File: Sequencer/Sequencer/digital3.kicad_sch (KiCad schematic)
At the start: 3 parts, among them U6 40106, U7 CD4094, U8 TL072

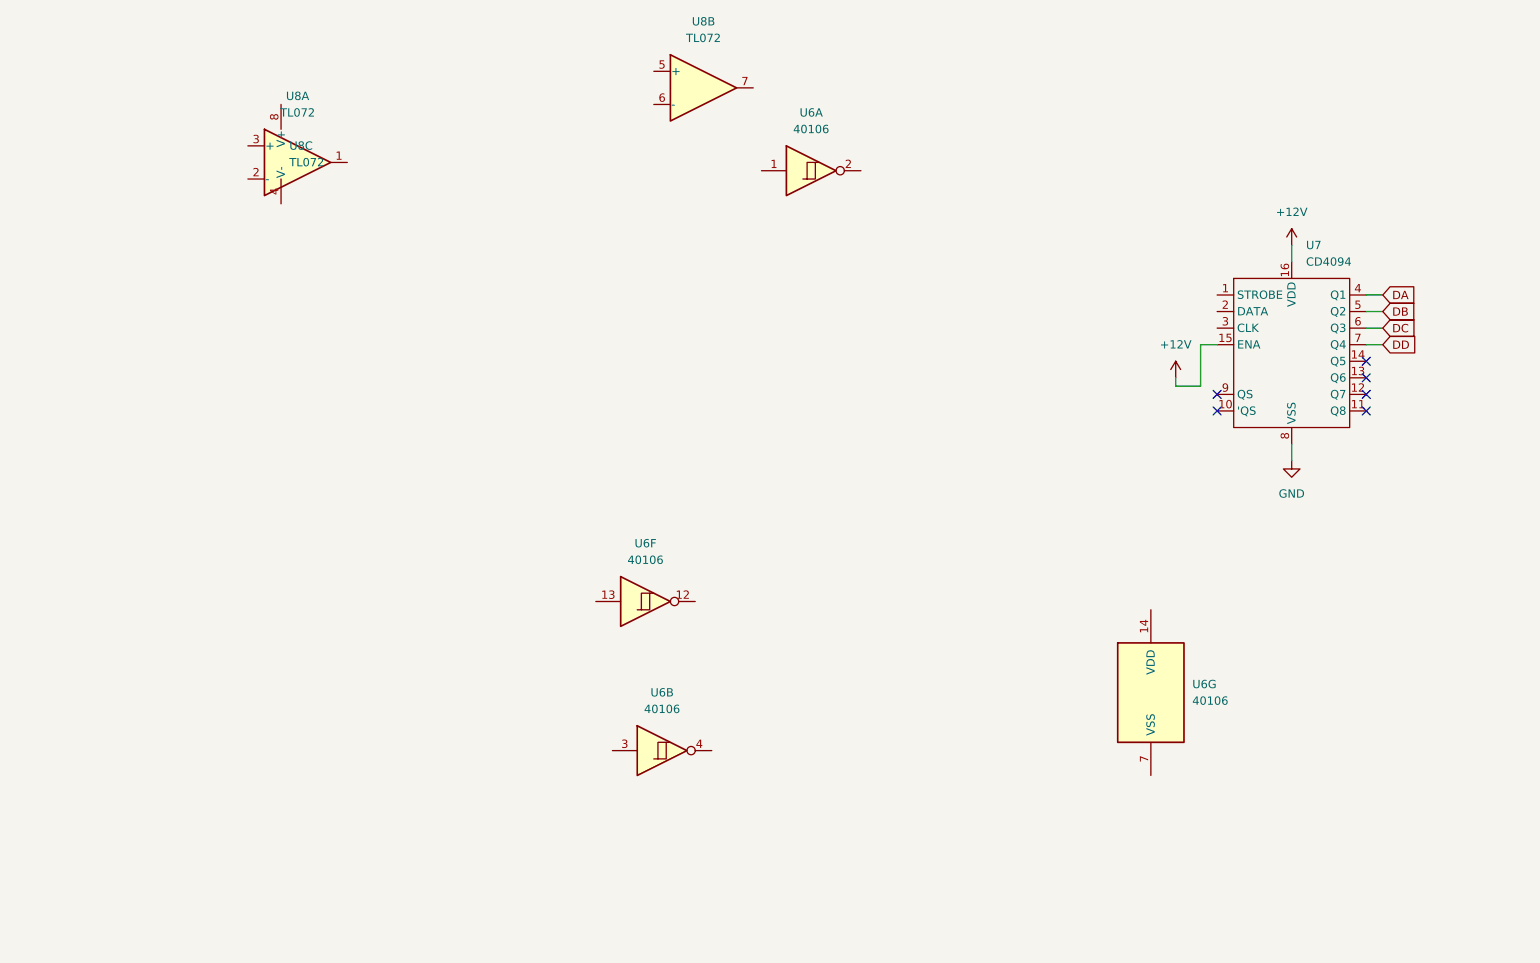
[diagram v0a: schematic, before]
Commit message: Sequencer - schematic mostly complete
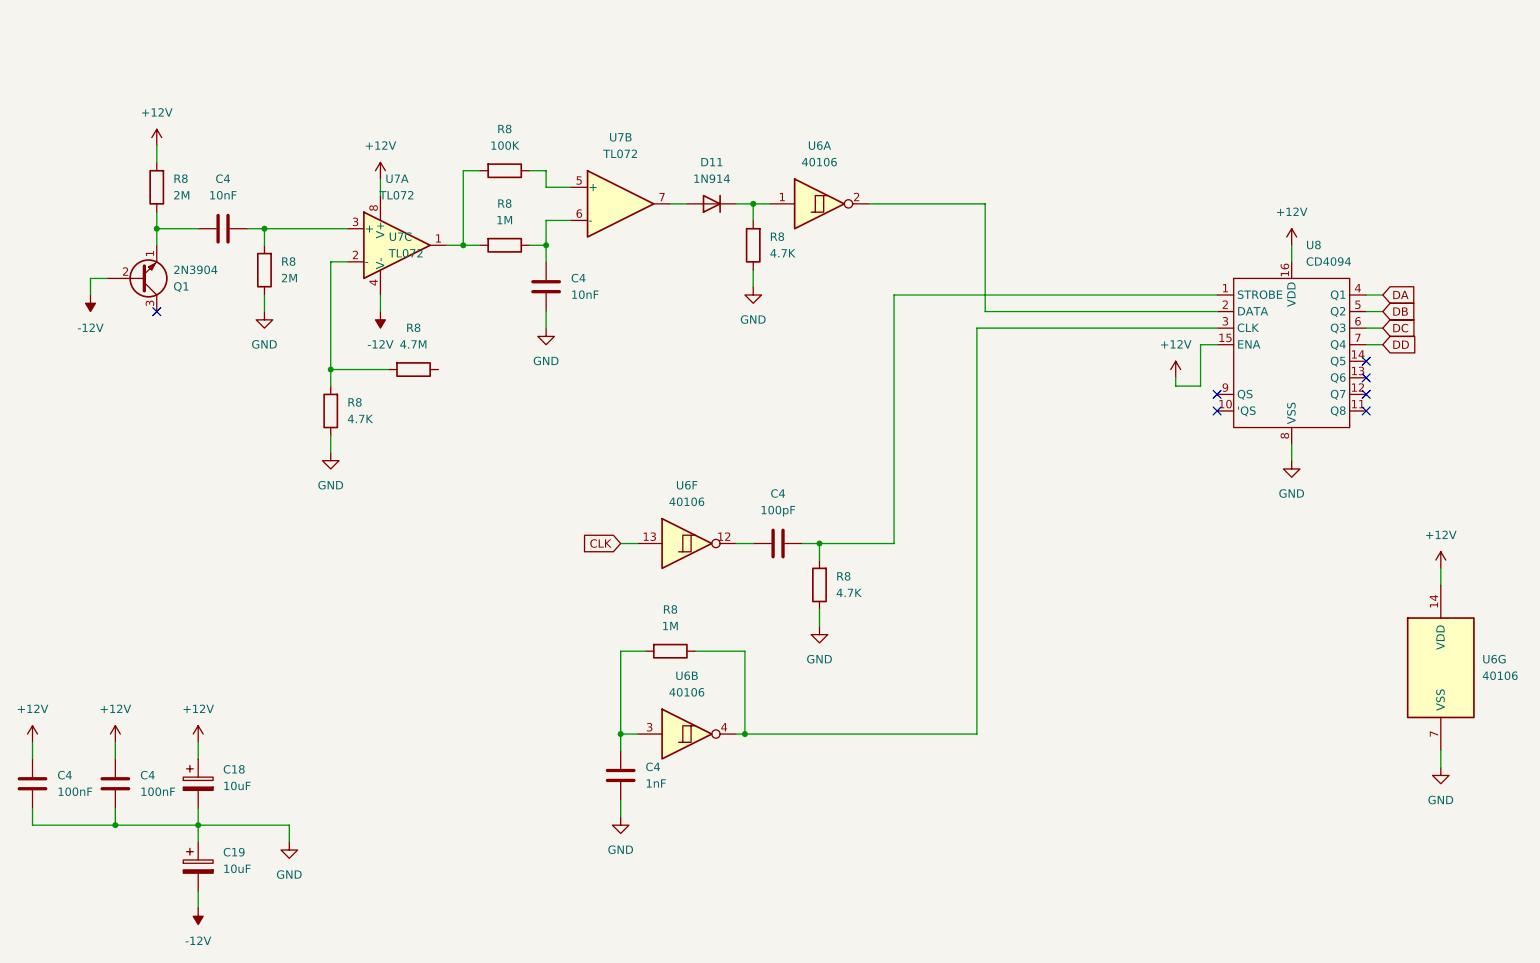
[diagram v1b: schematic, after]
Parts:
- added C18, C19: 10uF, Capacitor_THT:CP_Radial_D5.0mm_P2.50mm, symbol Device:C_Polarized
- added C4: 1nF, Capacitor_THT:C_Disc_D3.0mm_W1.6mm_P2.50mm, symbol Device:C
- added C4 (x2): 100nF, Capacitor_THT:C_Disc_D3.0mm_W1.6mm_P2.50mm, symbol Device:C
- added C4 (x2): 10nF, Capacitor_THT:C_Disc_D3.0mm_W1.6mm_P2.50mm, symbol Device:C
- added C4: 100pF, Capacitor_THT:C_Disc_D3.0mm_W1.6mm_P2.50mm, symbol Device:C
- added D11: 1N914, Diode_THT:D_DO-35_SOD27_P7.62mm_Horizontal, symbol Diode:1N914
- added Q1: 2N3904, Package_TO_SOT_THT:TO-92_Inline, symbol Transistor_BJT:2N3904
- added R8 (x2): 2M, Resistor_THT:R_Axial_DIN0207_L6.3mm_D2.5mm_P7.62mm_Horizontal, symbol Device:R
- added R8 (x2): 1M, Resistor_THT:R_Axial_DIN0207_L6.3mm_D2.5mm_P7.62mm_Horizontal, symbol Device:R
- added R8 (x3): 4.7K, Resistor_THT:R_Axial_DIN0207_L6.3mm_D2.5mm_P7.62mm_Horizontal, symbol Device:R
- added R8: 100K, Resistor_THT:R_Axial_DIN0207_L6.3mm_D2.5mm_P7.62mm_Horizontal, symbol Device:R
- added R8: 4.7M, Resistor_THT:R_Axial_DIN0207_L6.3mm_D2.5mm_P7.62mm_Horizontal, symbol Device:R
- U6: footprint (none) -> Package_DIP:DIP-14_W7.62mm_Socket_LongPads
- U7: renamed from U8; footprint (none) -> Package_DIP:DIP-8_W7.62mm_Socket_LongPads
- renumbered U7 to U8
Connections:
- net +12V: now also U6.14 (VDD), U7.8 (V+), C18.1, C4.2, C4.2, R8.2
- net GND: now also U6.7 (VSS), C18.2, C19.1, C4.1, C4.1, C4.1, C4.1, R8.1, R8.1, R8.1, R8.1
- net at U8.1 (STROBE): now also C4.2, R8.2
- net at U8.2 (DATA): now also U6.2
- net at U8.3 (CLK): now also U6.4, R8.1
- net at U6.1: now also D11.1 (K), R8.2
- net at U7.5 (+): now also R8.1
- net at U7.6 (-): now also C4.2, R8.1
- net at U7.7: now also D11.2 (A)
- net -12V: now reaches U7.4 (V-)
- net -12V: now also C19.2, Q1.2 (B)
- net at U6.3: now also C4.2, R8.2
- net at U6.12: now also C4.1
- net CLK: now reaches U6.13
- net at U7.1: now also R8.2, R8.2
- net at U7.2 (-): now also R8.2, R8.2
- net at U7.3 (+): now also C4.2, R8.2
- new net: C4.1, Q1.1 (E), R8.1
- no-connect marks 6 -> 7
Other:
- moved on the sheet: U6A, U6B, U6F, U6G, U7A, U7B, U7C

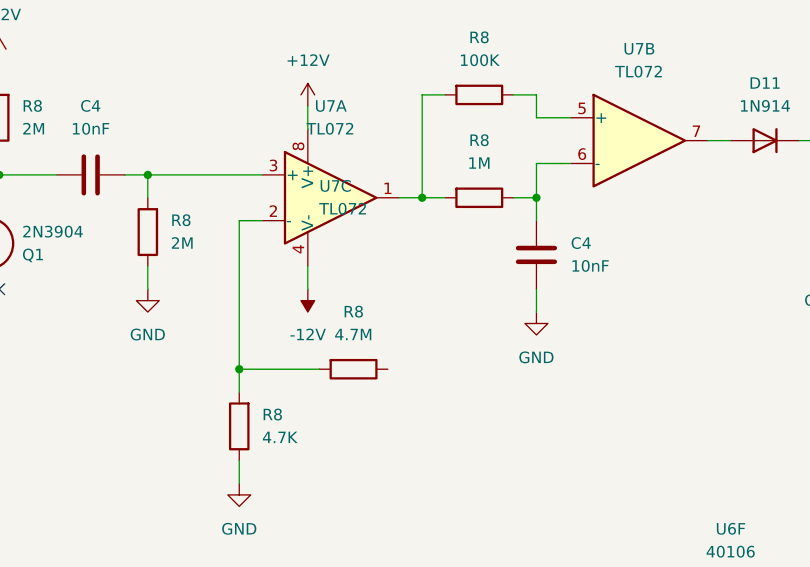
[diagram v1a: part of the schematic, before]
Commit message: Sequencer - minor progress on routing
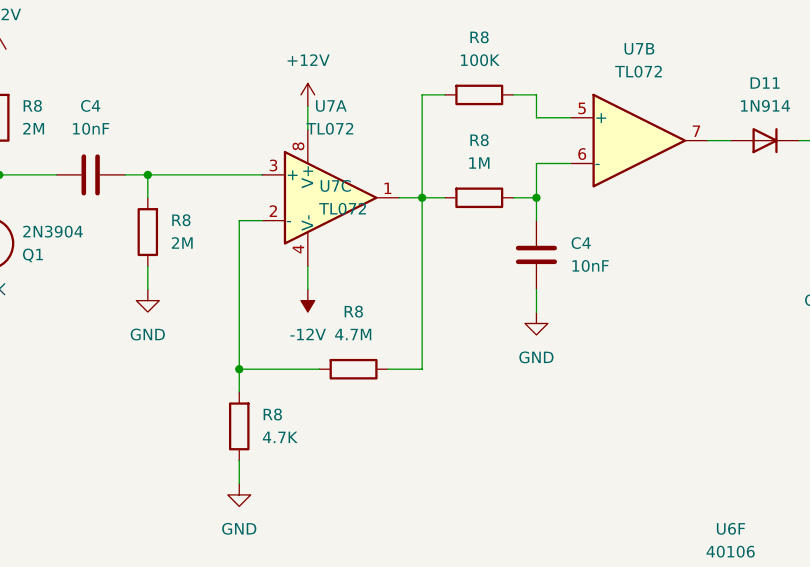
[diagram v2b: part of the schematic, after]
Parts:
- C4: footprint Capacitor_THT:C_Disc_D3.0mm_W1.6mm_P2.50mm -> Capacitor_THT:C_Disc_D5.0mm_W2.5mm_P2.50mm
- R8: footprint Resistor_THT:R_Axial_DIN0207_L6.3mm_D2.5mm_P7.62mm_Horizontal -> Library:R_Axial_DIN0207_L6.3mm_D2.5mm_P7.62mm_Horizontal
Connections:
- net at R8.2, R8.2, U7.1: now also R8.1
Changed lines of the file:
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@@
+    (stroke (width 0) (type default))
+  )
+  (wire (pts (xy 106.68 83.82) (xy 110.49 83.82))
     (stroke (width 0) (type default))
   )
@@
   )
   (wire (pts (xy 165.1 110.49) (xy 165.1 113.03))
+    (stroke (width 0) (type default))
+  )
+  (wire (pts (xy 110.49 83.82) (xy 110.49 64.77))
     (stroke (width 0) (type default))
   )
@@
       (effects (font (size 1.27 1.27)) (justify right))
     )
-    (property "Footprint" "Capacitor_THT:C_Disc_D3.0mm_W1.6mm_P2.50mm" (at 133.6548 142.24 0)
+    (property "Footprint" "Capacitor_THT:C_Disc_D5.0mm_W2.5mm_P2.50mm" (at 133.6548 142.24 0)
       (effects (font (size 1.27 1.27)) hide)
     )
@@
       (effects (font (size 1.27 1.27)) (justify right))
     )
-    (property "Footprint" "Resistor_THT:R_Axial_DIN0207_L6.3mm_D2.5mm_P7.62mm_Horizontal" (at 81.788 68.58 90)
+    (property "Footprint" "Library:R_Axial_DIN0207_L6.3mm_D2.5mm_P7.62mm_Horizontal" (at 81.788 68.58 90)
       (effects (font (size 1.27 1.27)) hide)
     )
@@
       (effects (font (size 1.27 1.27)) (justify right))
     )
-    (property "Footprint" "Capacitor_THT:C_Disc_D3.0mm_W1.6mm_P2.50mm" (at 56.1848 143.51 0)
+    (property "Footprint" "Capacitor_THT:C_Disc_D5.0mm_W2.5mm_P2.50mm" (at 56.1848 143.51 0)
       (effects (font (size 1.27 1.27)) hide)
     )
@@
       (effects (font (size 1.27 1.27)) (justify right))
     )
-    (property "Footprint" "Capacitor_THT:C_Disc_D3.0mm_W1.6mm_P2.50mm" (at 43.4848 143.51 0)
+    (property "Footprint" "Capacitor_THT:C_Disc_D5.0mm_W2.5mm_P2.50mm" (at 43.4848 143.51 0)
       (effects (font (size 1.27 1.27)) hide)
     )
@@
       (effects (font (size 1.27 1.27)))
     )
-    (property "Footprint" "Resistor_THT:R_Axial_DIN0207_L6.3mm_D2.5mm_P7.62mm_Horizontal" (at 142.24 125.222 90)
+    (property "Footprint" "Library:R_Axial_DIN0207_L6.3mm_D2.5mm_P7.62mm_Horizontal" (at 142.24 125.222 90)
       (effects (font (size 1.27 1.27)) hide)
     )
@@
       (effects (font (size 1.27 1.27)) (justify right))
     )
-    (property "Footprint" "Resistor_THT:R_Axial_DIN0207_L6.3mm_D2.5mm_P7.62mm_Horizontal" (at 91.948 90.17 90)
+    (property "Footprint" "Library:R_Axial_DIN0207_L6.3mm_D2.5mm_P7.62mm_Horizontal" (at 91.948 90.17 90)
       (effects (font (size 1.27 1.27)) hide)
     )
@@
       (effects (font (size 1.27 1.27)))
     )
-    (property "Footprint" "Resistor_THT:R_Axial_DIN0207_L6.3mm_D2.5mm_P7.62mm_Horizontal" (at 116.84 51.562 90)
+    (property "Footprint" "Library:R_Axial_DIN0207_L6.3mm_D2.5mm_P7.62mm_Horizontal" (at 116.84 51.562 90)
       (effects (font (size 1.27 1.27)) hide)
     )
@@
       (effects (font (size 1.27 1.27)) (justify right))
     )
-    (property "Footprint" "Capacitor_THT:C_Disc_D3.0mm_W1.6mm_P2.50mm" (at 122.2248 67.31 0)
+    (property "Footprint" "Capacitor_THT:C_Disc_D5.0mm_W2.5mm_P2.50mm" (at 122.2248 67.31 0)
       (effects (font (size 1.27 1.27)) hide)
     )
@@
       (effects (font (size 1.27 1.27)) (justify right))
     )
-    (property "Footprint" "Resistor_THT:R_Axial_DIN0207_L6.3mm_D2.5mm_P7.62mm_Horizontal" (at 156.718 64.77 90)
+    (property "Footprint" "Library:R_Axial_DIN0207_L6.3mm_D2.5mm_P7.62mm_Horizontal" (at 156.718 64.77 90)
       (effects (font (size 1.27 1.27)) hide)
     )
@@
       (effects (font (size 1.27 1.27)) (justify right))
     )
-    (property "Footprint" "Resistor_THT:R_Axial_DIN0207_L6.3mm_D2.5mm_P7.62mm_Horizontal" (at 65.278 55.88 90)
+    (property "Footprint" "Library:R_Axial_DIN0207_L6.3mm_D2.5mm_P7.62mm_Horizontal" (at 65.278 55.88 90)
       (effects (font (size 1.27 1.27)) hide)
     )
@@
       (effects (font (size 1.27 1.27)))
     )
-    (property "Footprint" "Resistor_THT:R_Axial_DIN0207_L6.3mm_D2.5mm_P7.62mm_Horizontal" (at 102.87 82.042 90)
+    (property "Footprint" "Library:R_Axial_DIN0207_L6.3mm_D2.5mm_P7.62mm_Horizontal" (at 102.87 82.042 90)
       (effects (font (size 1.27 1.27)) hide)
     )
@@
       (effects (font (size 1.27 1.27)))
     )
-    (property "Footprint" "Capacitor_THT:C_Disc_D3.0mm_W1.6mm_P2.50mm" (at 162.56 109.5248 0)
+    (property "Footprint" "Capacitor_THT:C_Disc_D5.0mm_W2.5mm_P2.50mm" (at 162.56 109.5248 0)
       (effects (font (size 1.27 1.27)) hide)
     )
@@
       (effects (font (size 1.27 1.27)) (justify right))
     )
-    (property "Footprint" "Resistor_THT:R_Axial_DIN0207_L6.3mm_D2.5mm_P7.62mm_Horizontal" (at 166.878 116.84 90)
+    (property "Footprint" "Library:R_Axial_DIN0207_L6.3mm_D2.5mm_P7.62mm_Horizontal" (at 166.878 116.84 90)
       (effects (font (size 1.27 1.27)) hide)
     )
@@
       (effects (font (size 1.27 1.27)))
     )
-    (property "Footprint" "Capacitor_THT:C_Disc_D3.0mm_W1.6mm_P2.50mm" (at 77.47 61.2648 0)
+    (property "Footprint" "Capacitor_THT:C_Disc_D5.0mm_W2.5mm_P2.50mm" (at 77.47 61.2648 0)
       (effects (font (size 1.27 1.27)) hide)
     )
@@
       (effects (font (size 1.27 1.27)))
     )
-    (property "Footprint" "Resistor_THT:R_Axial_DIN0207_L6.3mm_D2.5mm_P7.62mm_Horizontal" (at 116.84 62.992 90)
-      (effects (font (size 1.27 1.27)) hide)
-    )
+    (property "Footprint" "Library:R_Axial_DIN0207_L6.3mm_D2.5mm_P7.62mm_Horizontal" (at 116.84 62.992 90)
+      (effects (font (size 1.27 1.27)) hide)
+    )
